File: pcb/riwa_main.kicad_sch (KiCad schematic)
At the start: 13 parts

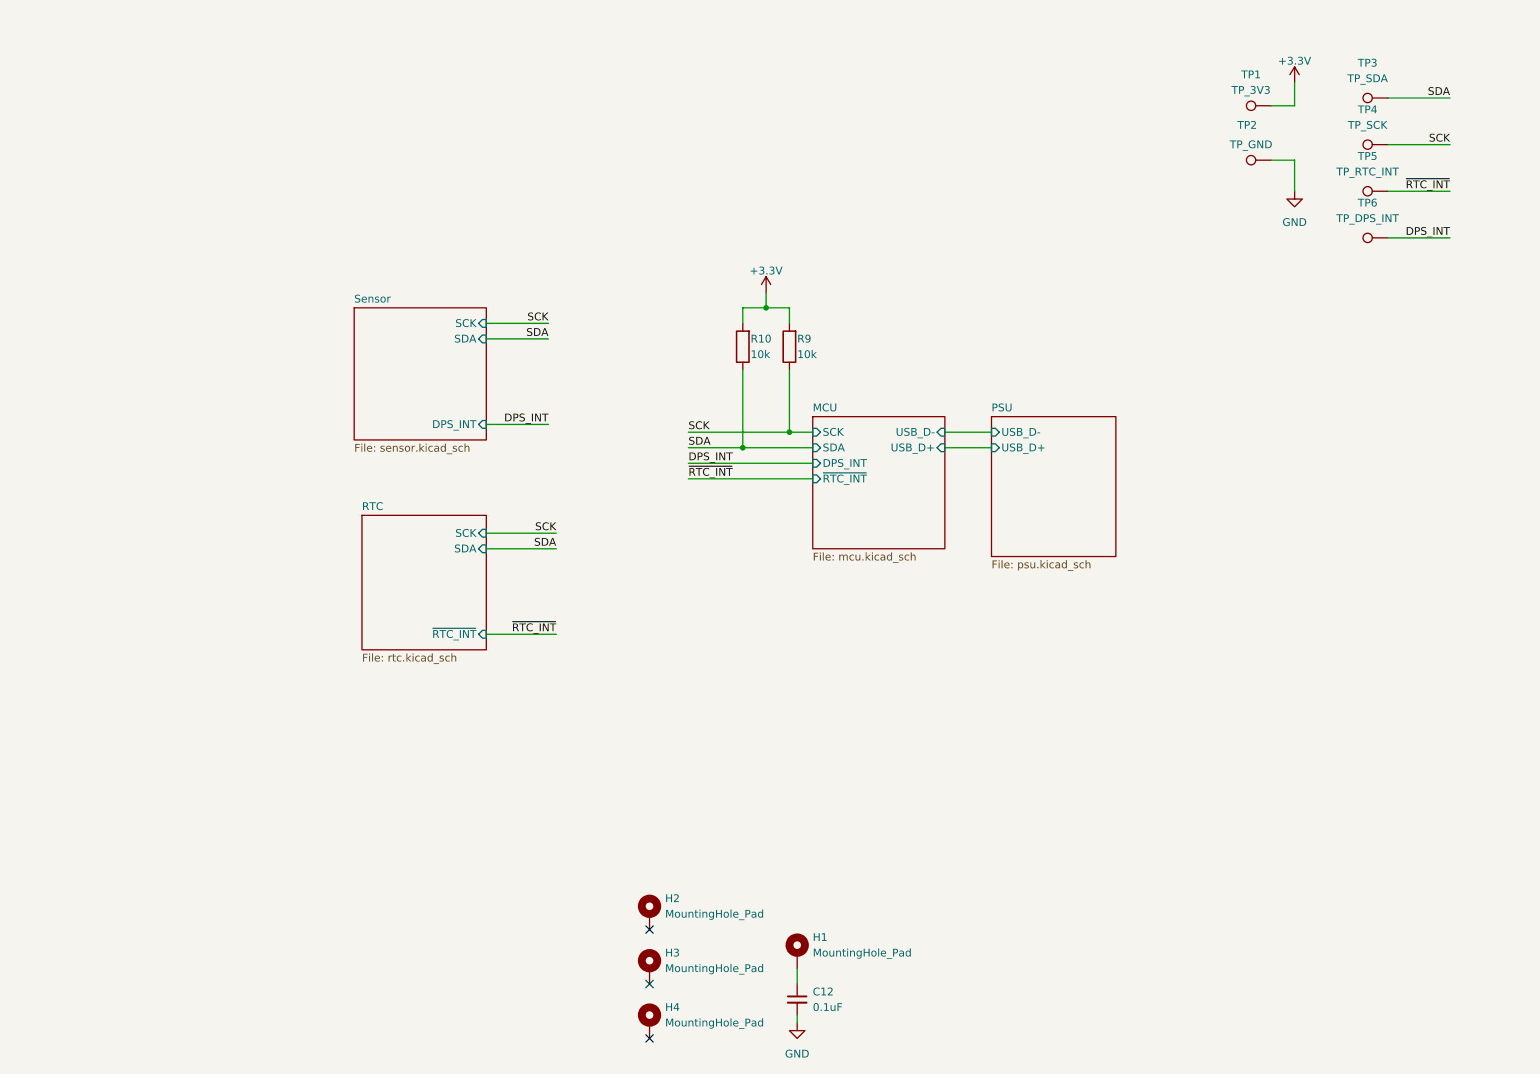
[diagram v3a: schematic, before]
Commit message: Refactored layout + silkscreen + added I2C connector
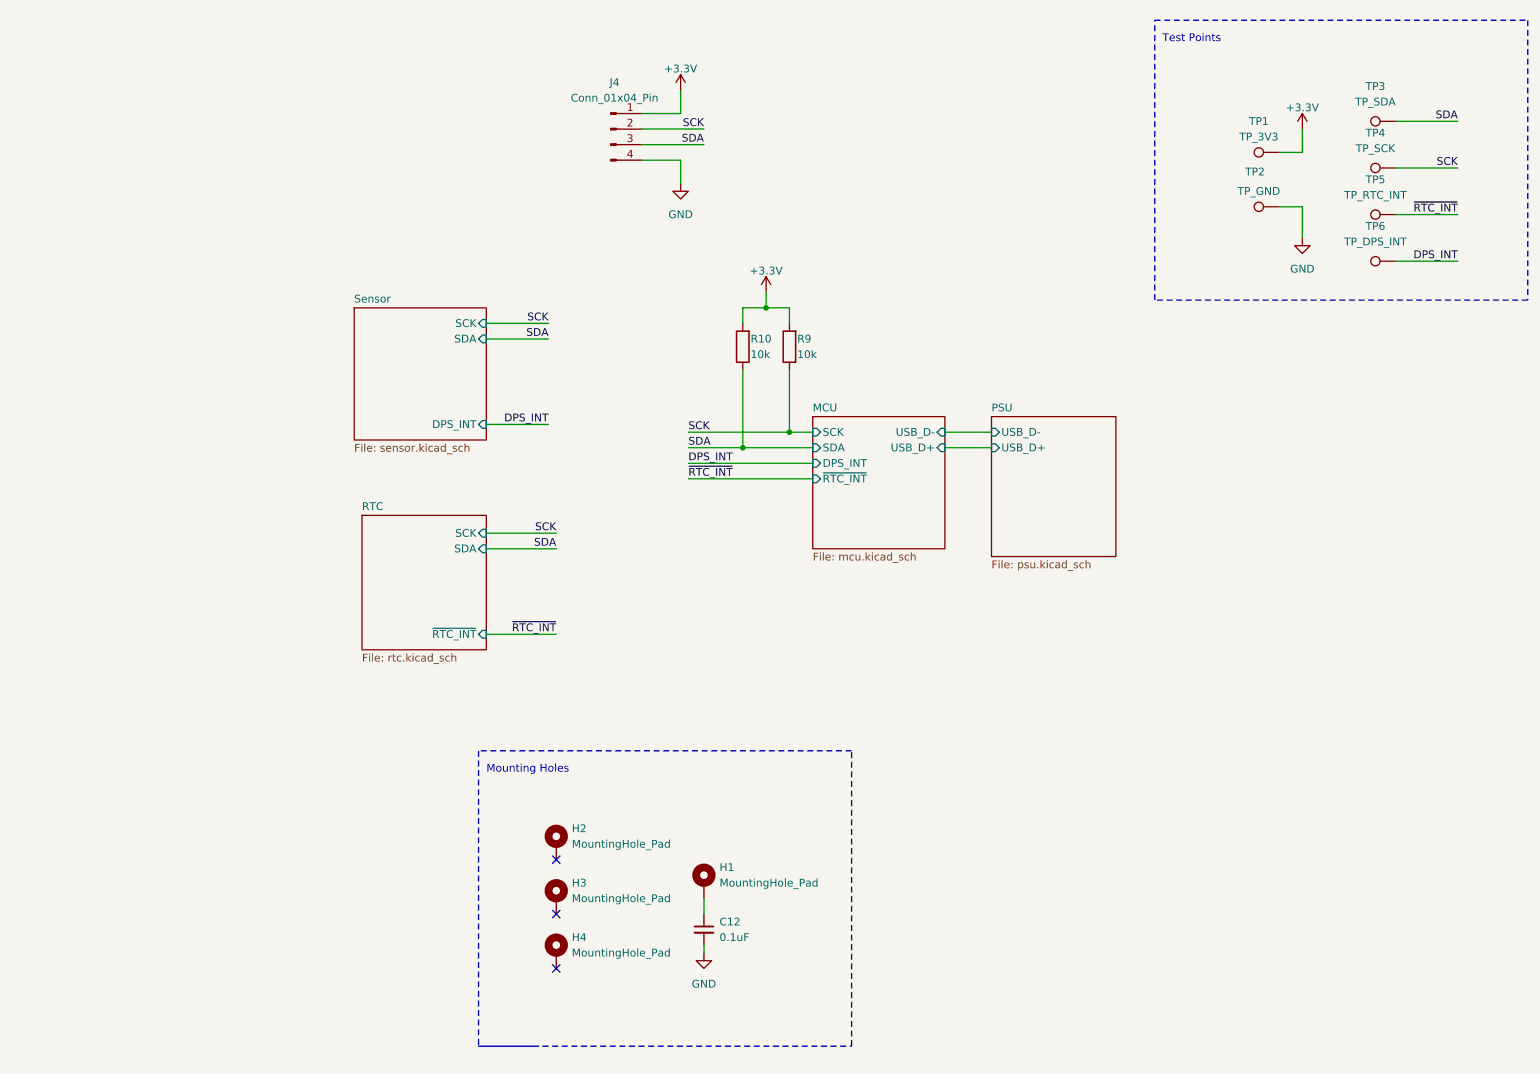
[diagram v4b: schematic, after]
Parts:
- added J4: Conn_01x04_Pin, Connector_PinSocket_2.54mm:PinSocket_1x04_P2.54mm_Vertical, symbol Connector:Conn_01x04_Pin
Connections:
- net +3.3V: now also J4.1 (Pin_1)
- net GND: now also J4.4 (Pin_4)
- net SCK: now also J4.2 (Pin_2)
- net SDA: now also J4.3 (Pin_3)
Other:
- note added: "Mounting Holes"
- note added: "Test Points"
- moved on the sheet: C12, H1, H2, H3, H4, TP1, TP2, TP3, TP4, TP5, TP6

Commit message: Implement RTC and device sync + updated 3d objects
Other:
- sheet MCU ports: added VBUS_DETECT; removed none
- sheet PSU ports: added VBUS_DETECT; removed none
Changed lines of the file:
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@@
     (stroke (width 0) (type default))
   )
-  (wire (pts (xy 179.07 88.9) (xy 186.69 88.9))
+  (wire (pts (xy 186.69 88.9) (xy 201.93 88.9))
     (stroke (width 0) (type default))
   )
@@
     (stroke (width 0) (type dash))
   )
+  (wire (pts (xy 186.69 93.98) (xy 201.93 93.98))
+    (stroke (width 0) (type default))
+  )
   (wire (pts (xy 135.89 44.45) (xy 129.54 44.45))
     (stroke (width 0) (type default))
@@
     (stroke (width 0) (type default))
   )
-  (wire (pts (xy 179.07 91.44) (xy 186.69 91.44))
+  (wire (pts (xy 186.69 91.44) (xy 201.93 91.44))
     (stroke (width 0) (type default))
   )
@@
     )
   )
-  (sheet (at 157.48 86.36) (size 21.59 21.59) (fields_autoplaced)
+  (sheet (at 157.48 86.36) (size 29.21 21.59) (fields_autoplaced)
     (stroke (width 0.1524) (type solid))
     (fill (color 0 0 0 0.0000))
@@
       (effects (font (size 1.27 1.27)) (justify left))
     )
-    (pin "USB_D-" input (at 179.07 88.9 0)
+    (pin "USB_D-" input (at 186.69 88.9 0)
       (effects (font (size 1.27 1.27)) (justify right))
     )
@@
       (effects (font (size 1.27 1.27)) (justify left))
     )
-    (pin "USB_D+" input (at 179.07 91.44 0)
+    (pin "USB_D+" input (at 186.69 91.44 0)
+      (effects (font (size 1.27 1.27)) (justify right))
+    )
+    (pin "VBUS_DETECT" input (at 186.69 93.98 0)
       (effects (font (size 1.27 1.27)) (justify right))
     )
@@
     )
   )
-  (sheet (at 186.69 86.36) (size 20.32 22.86) (fields_autoplaced)
+  (sheet (at 201.93 86.36) (size 20.32 22.86) (fields_autoplaced)
     (stroke (width 0.1524) (type solid))
     (fill (color 0 0 0 0.0000))
-    (property "Sheetname" "PSU" (at 186.69 85.6484 0)
+    (property "Sheetname" "PSU" (at 201.93 85.6484 0)
       (effects (font (size 1.27 1.27)) (justify left bottom))
     )
-    (property "Sheetfile" "psu.kicad_sch" (at 186.69 109.8046 0)
+    (property "Sheetfile" "psu.kicad_sch" (at 201.93 109.8046 0)
       (effects (font (size 1.27 1.27)) (justify left top))
     )
-    (pin "USB_D-" input (at 186.69 88.9 180)
-      (effects (font (size 1.27 1.27)) (justify left))
-    )
-    (pin "USB_D+" input (at 186.69 91.44 180)
-      (effects (font (size 1.27 1.27)) (justify left))
-    )
+    (pin "USB_D-" input (at 201.93 88.9 180)
+      (effects (font (size 1.27 1.27)) (justify left))
+    )
+    (pin "USB_D+" input (at 201.93 91.44 180)
+      (effects (font (size 1.27 1.27)) (justify left))
+    )
+    (pin "VBUS_DETECT" input (at 201.93 93.98 180)
+      (effects (font (size 1.27 1.27)) (justify left))
+    )
